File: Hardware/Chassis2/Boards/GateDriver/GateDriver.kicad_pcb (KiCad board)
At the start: 6 copper layers, 260 x 45 mm, 155 parts, among them IC1 NCD57100DWR2G, IC2 NCD57100DWR2G, IC3 NCD57100DWR2G, IC4 NCD57100DWR2G, IC5 NCD57100DWR2G, IC6 NCD57100DWR2G, J1 Conn_02x08_Counter_Clockwise, J2 TBP01R2W-508-06BE, J3 TBP01R2W-508-06BE, J4 TBP01R2W-508-06BE, U5 BTS462TATMA1

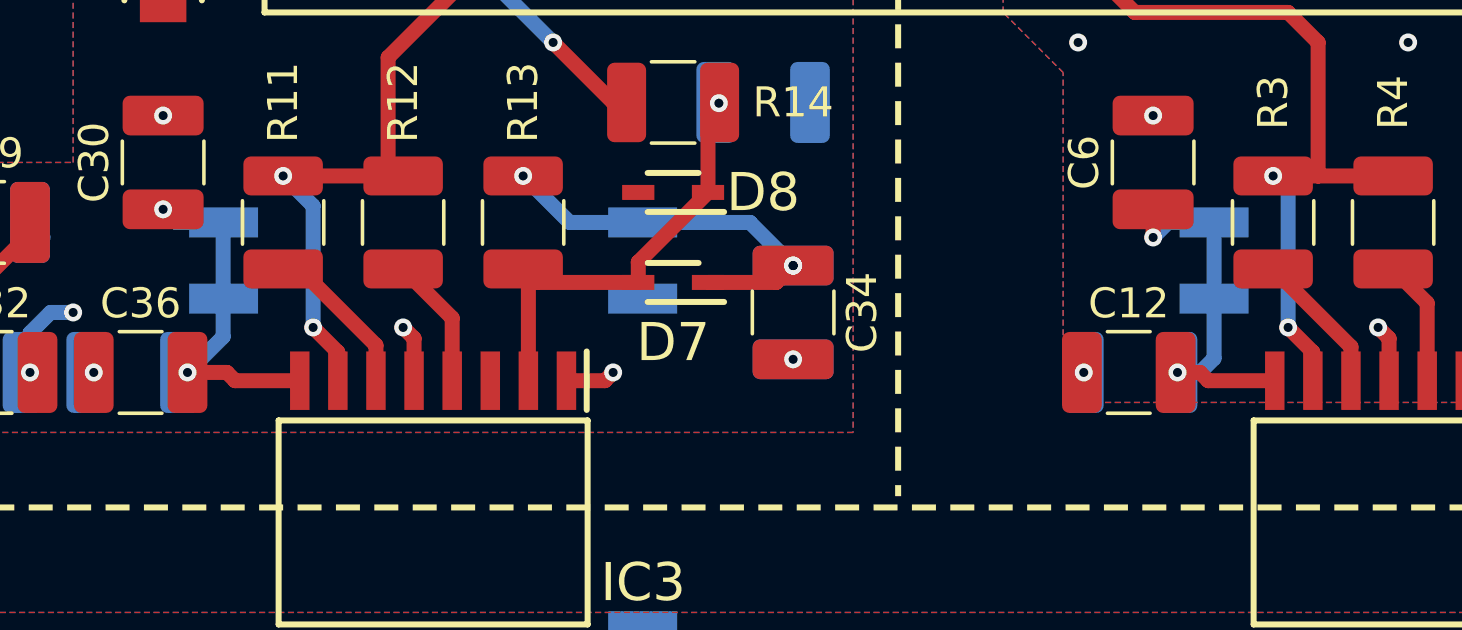
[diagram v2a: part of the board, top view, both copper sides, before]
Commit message: Update mechanical model for new gate driver
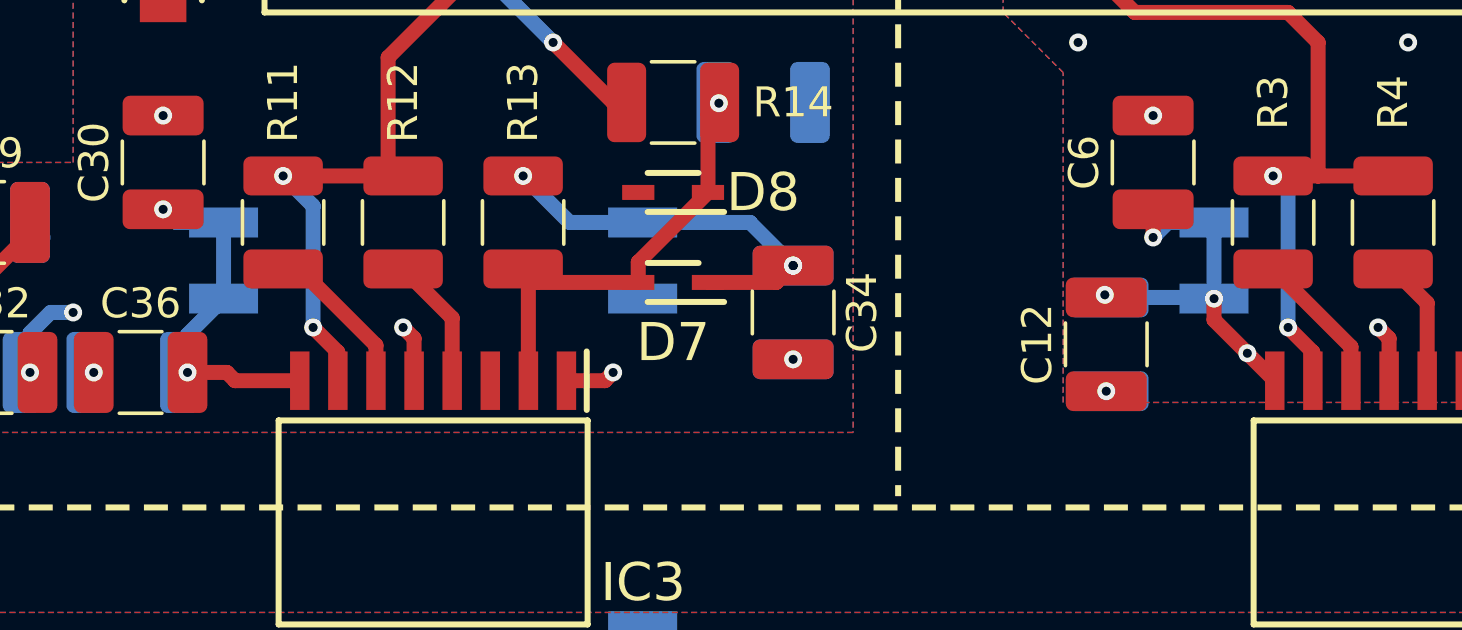
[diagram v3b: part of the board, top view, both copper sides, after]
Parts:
- moved C12 1.20 mm to (47.4, 22.1), turned to 90 degrees
- moved C7 1.20 mm to (47.5, 22.1), turned to 90 degrees
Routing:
- net /SingleChannelDriver1/-9V_B: track 13.6 -> 14.0 mm, vias 6 -> 8
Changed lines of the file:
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@@
 	(footprint "Capacitor_SMD:C_1210_3225Metric_Pad1.33x2.70mm_HandSolder"
 		(layer "F.Cu")
-		(at 48.1875 23)
+		(at 47.4375 22.0625 90)
 		(descr "Capacitor SMD 1210 (3225 Metric), square (rectangular) end terminal, IPC-7351 nominal with elongated pad for handsoldering. (Body size source: IPC-SM-782 page 76, https://www.pcb-3d.com/wordpress/wp-content/uploads/ipc-sm-782a_amendment_1_and_2.pdf), generated with kicad-footprint-generator")
 		(tags "capacitor handsolder")
 		(property "Reference" "C12"
-			(at 0 -2.3 0)
+			(at 0 -2.3 90)
 			(layer "F.SilkS")
 			(effects
@@
 		)
 		(property "Value" "10uF"
-			(at 0 2.3 0)
+			(at 0 2.3 90)
 			(layer "F.Fab")
 			(effects
@@
 		)
 		(property "Datasheet" ""
-			(at 0 0 0)
+			(at 0 0 90)
 			(layer "F.Fab")
 			(hide yes)
@@
 		)
 		(property "Description" "Unpolarized capacitor"
-			(at 0 0 0)
+			(at 0 0 90)
 			(layer "F.Fab")
 			(hide yes)
@@
 		)
 		(fp_line
-			(start -2.48 -1.6)
-			(end 2.48 -1.6)
+			(start 2.48 -1.6)
+			(end 2.48 1.6)
 			(stroke
 				(width 0.05)
@@
 		)
 		(fp_line
-			(start -2.48 1.6)
-			(end -2.48 -1.6)
+			(start -2.48 -1.6)
+			(end 2.48 -1.6)
 			(stroke
 				(width 0.05)
@@
 		)
 		(fp_line
-			(start 2.48 -1.6)
-			(end 2.48 1.6)
+			(start 2.48 1.6)
+			(end -2.48 1.6)
 			(stroke
 				(width 0.05)
@@
 		)
 		(fp_line
-			(start 2.48 1.6)
-			(end -2.48 1.6)
+			(start -2.48 1.6)
+			(end -2.48 -1.6)
 			(stroke
 				(width 0.05)
@@
 		)
 		(fp_line
-			(start -1.6 -1.25)
-			(end 1.6 -1.25)
+			(start 1.6 -1.25)
+			(end 1.6 1.25)
 			(stroke
 				(width 0.1)
@@
 		)
 		(fp_line
-			(start -1.6 1.25)
-			(end -1.6 -1.25)
+			(start -1.6 -1.25)
+			(end 1.6 -1.25)
 			(stroke
 				(width 0.1)
@@
 		)
 		(fp_line
-			(start 1.6 -1.25)
-			(end 1.6 1.25)
+			(start 1.6 1.25)
+			(end -1.6 1.25)
 			(stroke
 				(width 0.1)
@@
 		)
 		(fp_line
-			(start 1.6 1.25)
-			(end -1.6 1.25)
+			(start -1.6 1.25)
+			(end -1.6 -1.25)
 			(stroke
 				(width 0.1)
@@
 		)
 		(fp_text user "${REFERENCE}"
-			(at 0 0 0)
+			(at 0 0 90)
 			(layer "F.Fab")
 			(effects
@@
 		)
 		(pad "1" smd roundrect
-			(at -1.5625 0)
+			(at -1.5625 0 90)
 			(size 1.325 2.7)
 			(layers "F.Cu" "F.Mask" "F.Paste")
@@
 		)
 		(pad "2" smd roundrect
-			(at 1.5625 0)
+			(at 1.5625 0 90)
 			(size 1.325 2.7)
 			(layers "F.Cu" "F.Mask" "F.Paste")
@@
 	)
 	(footprint "Connector_PinHeader_2.54mm:PinHeader_2x08_P2.54mm_Vertical"
+		(locked yes)
 		(layer "F.Cu")
 		(at 125.38 42.54 90)
@@
 	(footprint "Capacitor_SMD:C_1210_3225Metric_Pad1.33x2.70mm_HandSolder"
 		(layer "B.Cu")
-		(at 48.25 23)
+		(at 47.5 22.0625 90)
 		(descr "Capacitor SMD 1210 (3225 Metric), square (rectangular) end terminal, IPC-7351 nominal with elongated pad for handsoldering. (Body size source: IPC-SM-782 page 76, https://www.pcb-3d.com/wordpress/wp-content/uploads/ipc-sm-782a_amendment_1_and_2.pdf), generated with kicad-footprint-generator")
 		(tags "capacitor handsolder")
 		(property "Reference" "C7"
-			(at 0 2.3 0)
+			(at 0 2.3 90)
 			(layer "B.SilkS")
 			(effects
@@
 		)
 		(property "Value" "10uF"
-			(at 0 -2.3 0)
+			(at 0 -2.3 90)
 			(layer "B.Fab")
 			(effects
@@
 		)
 		(property "Datasheet" ""
-			(at 0 0 0)
+			(at 0 0 90)
 			(layer "B.Fab")
 			(hide yes)
@@
 		)
 		(property "Description" "Unpolarized capacitor"
-			(at 0 0 0)
+			(at 0 0 90)
 			(layer "B.Fab")
 			(hide yes)
@@
 		)
 		(fp_line
-			(start -2.48 -1.6)
-			(end -2.48 1.6)
+			(start 2.48 -1.6)
+			(end -2.48 -1.6)
 			(stroke
 				(width 0.05)
@@
 		)
 		(fp_line
-			(start -2.48 1.6)
-			(end 2.48 1.6)
+			(start -2.48 -1.6)
+			(end -2.48 1.6)
 			(stroke
 				(width 0.05)
@@
 		)
 		(fp_line
-			(start 2.48 -1.6)
-			(end -2.48 -1.6)
+			(start 2.48 1.6)
+			(end 2.48 -1.6)
 			(stroke
 				(width 0.05)
@@
 		)
 		(fp_line
-			(start 2.48 1.6)
-			(end 2.48 -1.6)
+			(start -2.48 1.6)
+			(end 2.48 1.6)
 			(stroke
 				(width 0.05)
@@
 		)
 		(fp_line
-			(start -1.6 -1.25)
-			(end -1.6 1.25)
+			(start 1.6 -1.25)
+			(end -1.6 -1.25)
 			(stroke
 				(width 0.1)
@@
 		)
 		(fp_line
-			(start -1.6 1.25)
-			(end 1.6 1.25)
+			(start -1.6 -1.25)
+			(end -1.6 1.25)
 			(stroke
 				(width 0.1)
@@
 		)
 		(fp_line
-			(start 1.6 -1.25)
-			(end -1.6 -1.25)
+			(start 1.6 1.25)
+			(end 1.6 -1.25)
 			(stroke
 				(width 0.1)
@@
 		)
 		(fp_line
-			(start 1.6 1.25)
-			(end 1.6 -1.25)
+			(start -1.6 1.25)
+			(end 1.6 1.25)
 			(stroke
 				(width 0.1)
@@
 		)
 		(fp_text user "${REFERENCE}"
-			(at 0 0 0)
+			(at 0 0 90)
 			(layer "B.Fab")
 			(effects
@@
 		)
 		(pad "1" smd roundrect
-			(at -1.5625 0)
+			(at -1.5625 0 90)
 			(size 1.325 2.7)
 			(layers "B.Cu" "B.Mask" "B.Paste")
@@
 		)
 		(pad "2" smd roundrect
-			(at 1.5625 0)
+			(at 1.5625 0 90)
 			(size 1.325 2.7)
 			(layers "B.Cu" "B.Mask" "B.Paste")
@@
 	)
 	(via
-		(at 46.6875 23)
+		(at 47.4375 23.625)
 		(size 0.6)
 		(drill 0.3)
@@
 	)
 	(segment
-		(start 50.5625 23)
-		(end 50.8375 23.275)
-		(width 0.5)
-		(layer "F.Cu")
-		(net 6)
-	)
-	(segment
-		(start 49.8125 23)
-		(end 50.5625 23)
+		(start 51.03 21.25)
+		(end 52.14 22.36)
 		(width 0.5)
 		(layer "F.Cu")
@@
 	)
 	(segment
-		(start 50.8375 23.275)
+		(start 51.03 20.54)
+		(end 51.03 21.25)
+		(width 0.5)
+		(layer "F.Cu")
+		(net 6)
+	)
+	(segment
+		(start 52.14 22.36)
 		(end 53.055 23.275)
 		(width 0.5)
@@
 	)
 	(via
-		(at 49.8125 23)
+		(at 51.03 20.54)
 		(size 0.6)
 		(drill 0.3)
@@
 	)
 	(via
+		(at 47.389702 20.413238)
+		(size 0.6)
+		(drill 0.3)
+		(layers "F.Cu" "B.Cu")
+		(net 6)
+	)
+	(via
 		(at 69 23.5625)
 		(size 0.6)
@@
 	)
 	(via
+		(at 52.14 22.36)
+		(size 0.6)
+		(drill 0.3)
+		(layers "F.Cu" "B.Cu")
+		(net 6)
+	)
+	(via
 		(at 76.5625 16)
 		(size 0.6)
@@
 	)
 	(segment
-		(start 49.5 18)
-		(end 49 18.5)
-		(width 0.5)
-		(layer "B.Cu")
-		(net 6)
-	)
-	(segment
-		(start 51.03 22.5325)
+		(start 50.99 20.5)
 		(end 51.03 20.54)
 		(width 0.5)
@@
 	)
 	(segment
-		(start 49.8125 23)
-		(end 50.5625 23)
+		(start 49.5 18)
+		(end 49 18.5)
 		(width 0.5)
 		(layer "B.Cu")
@@
 	)
 	(segment
-		(start 50.5625 23)
-		(end 51.03 22.5325)
+		(start 47.5 20.5)
+		(end 50.99 20.5)
 		(width 0.5)
 		(layer "B.Cu")
@@
 	)
 	(segment
-		(start 18 18.015)
-		(end 18.015 18)
-		(width 0.5)
-		(layer "B.Cu")
-		(net 10)
-	)
-	(segment
 		(start 11.5625 21.6875)
 		(end 12.25 21)
@@
 	)
 	(segment
-		(start 16.8125 23)
-		(end 18 21.8125)
+		(start 18.015 20.54)
+		(end 18.015 18)
 		(width 0.5)
 		(layer "B.Cu")
@@
 	)
 	(segment
-		(start 18 21.8125)
-		(end 18 18.015)
+		(start 18.015 18)
+		(end 16.4375 18)
 		(width 0.5)
 		(layer "B.Cu")
@@
 	)
 	(segment
-		(start 18.015 18)
-		(end 16.4375 18)
+		(start 16.8125 23)
+		(end 16.8125 21.7425)
 		(width 0.5)
 		(layer "B.Cu")
@@
 		(width 0.5)
 		(layer "B.Cu")
+		(net 10)
+	)
+	(segment
+		(start 16.8125 21.7425)
+		(end 18.015 20.54)
+		(width 0.5)
+		(layer "B.Cu")

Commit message: fix spacing and coupling isssues on pcbs
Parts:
- moved TP1 1.50 mm to (36.0, 35.5)
- moved LED2 1.35 mm to (231.5, 42.2)
- moved C14 1.06 mm to (127.1, 32.5), turned to 180 degrees
- moved C15 1.00 mm to (127.0, 32.5), turned to 0 degrees
- moved TP3 1.00 mm to (47.0, 36.0)
- moved R2 0.56 mm to (231.8, 42.5)
- moved TP2 0.50 mm to (41.0, 33.5)
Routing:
- net /READY: track 286.8 -> 291.8 mm, vias 9 -> 11
- net /PH_W_H: track 116.1 -> 113.0 mm
- net /PH_W_L: track 120.4 -> 118.7 mm
- net /FAULT: track 273.3 -> 275.0 mm, vias 7 -> 9
- net Net-(LED2-A): track 1.75 -> 0.33 mm
- net /+3.3V_A: track 20.7 -> 19.6 mm
- net /PH_U_L: track 131.9 -> 131.2 mm
- net /PH_V_L: track 47.0 -> 47.7 mm
- net /GND_A: vias 38 -> 37
